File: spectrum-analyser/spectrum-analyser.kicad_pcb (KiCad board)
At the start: 2 copper layers, 37 parts, among them J1 Conn_Coaxial, J2 Conn_01x02, Q1 PMOS, Q2 PMOS, Q3 Q_NMOS_GSD, Q4 Q_NMOS_GSD, Q5 Q_PMOS_GSD, SW2 SW_UP, SW3 SW_RIGHT, SW4 SW_LEFT, SW5 SW_DOWN, SW6 SW_SPDT, U1 1.3" OLED, U2 LM1117MP-3.3, U3 ESP32-C3_Zero, U4 RX5808(V3.3), U5 AP9101CK6, U6 MCP73831-2-OT

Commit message: Improve PCB layout
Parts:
- JP1: value SolderJumper_2_Open -> BAT_PROT_BYPASS; footprint Jumper:SolderJumper-2_P1.3mm_Open_RoundedPad1.0x1.5mm -> Jumper:SolderJumper-3_P1.3mm_Open_RoundedPad1.0x1.5mm
- moved R8 144.8 mm to (102.5, 125.5)
- moved U6 144.8 mm to (99.5, 125.5)
- moved J2 134.9 mm to (99.0, 100.2), turned to 0 degrees
- moved JP1 131.4 mm to (99.0, 106.5)
- moved F1 126.8 mm to (105.5, 107.5), turned to 180 degrees
- moved Q4 124.1 mm to (101.5, 113.0), turned to -90 degrees
- moved R7 121.8 mm to (105.5, 111.0), turned to 0 degrees
- moved R6 121.0 mm to (105.5, 119.0), turned to 0 degrees
- moved Q5 119.6 mm to (101.5, 117.0)
- moved C3 119.3 mm to (105.5, 113.0), turned to 0 degrees
- moved U5 118.6 mm to (105.5, 116.0), turned to 0 degrees
- moved TP1 114.8 mm to (129.0, 151.5)
- moved TP2 109.9 mm to (125.5, 121.0)
- moved TP3 109.7 mm to (125.5, 125.5)
- moved SW1 101.4 mm to (142.6, 79.0)
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- renumbered D3 to D1, D1 to D2, D2 to D3, Q5 to Q3, Q3 to Q4, Q4 to Q5, R7 to R1, R8 to R3, R1 to R4, R3 to R5, R4 to R6, R5 to R7, R6 to R8, SW6 to SW1, U3 to U2, U2 to U3
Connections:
- C3 pad 1: -BATT -> -BAT_PROT
- JP1 pad 1: -BATT -> -BAT_PROT
- JP1 pad 2: GND -> -BATT
- Q4 pad 2: -BATT -> -BAT_PROT
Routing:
- added copper zone on B.Cu, net GND
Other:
- board outline added: 50 x 90 mm
- board text added: "3V3 REG"
- board text added: "BAT_PROT"
- board text added: "CHRG"
- board text added: "PCBWay max board size 50x110mm"
- board text added: "VUSB"
- board text removed: "PCBWay max board size"

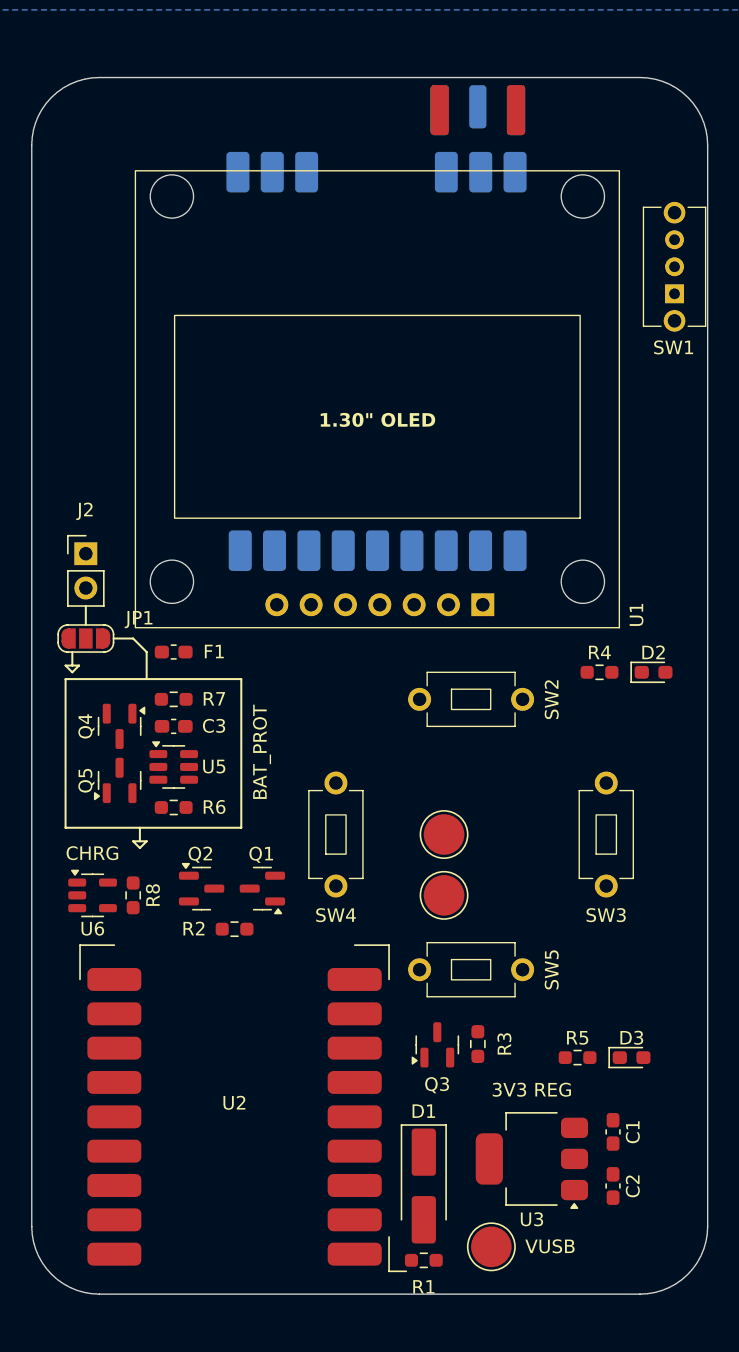
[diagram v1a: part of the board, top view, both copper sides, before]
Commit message: Add mounting holes
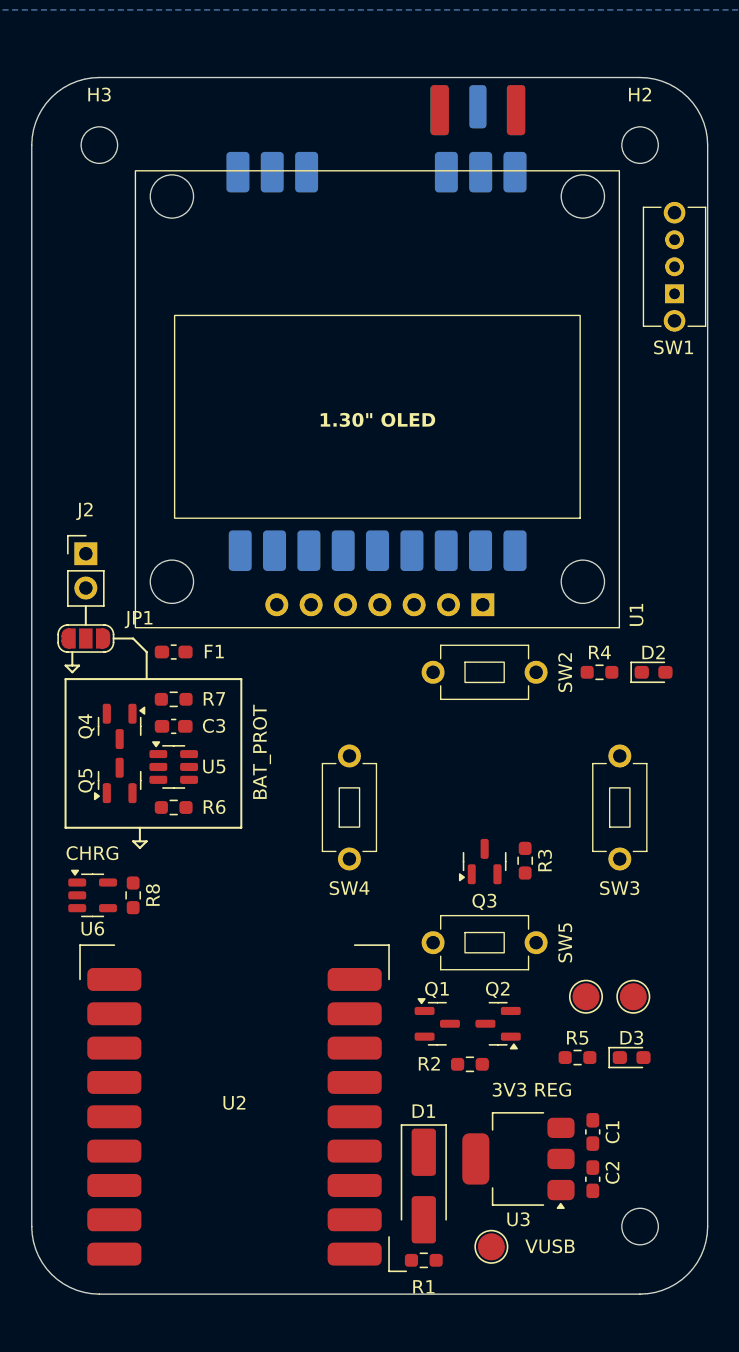
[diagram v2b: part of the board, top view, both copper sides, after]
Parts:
- added H1: MountingHole, MountingHole:MountingHole_2.7mm_M2.5, F.Cu at (140.0, 150.0)
- added H2: MountingHole, MountingHole:MountingHole_2.7mm_M2.5, F.Cu at (140.0, 70.0)
- added H3: MountingHole, MountingHole:MountingHole_2.7mm_M2.5, F.Cu at (100.0, 70.0)
- TP1, TP2, TP3: footprint TestPoint:TestPoint_Pad_D3.0mm -> TestPoint:TestPoint_Pad_D2.0mm
- moved Q1 20.1 mm to (125.0, 135.0)
- moved Q2 20.1 mm to (129.5, 135.0)
- moved R2 20.1 mm to (127.4, 138.0)
- moved TP2 15.9 mm to (136.0, 133.0)
- moved TP3 15.9 mm to (139.5, 133.0)
- moved Q3 14.0 mm to (128.5, 123.0)
- moved R3 14.0 mm to (131.5, 122.9)
- moved SW2 2.24 mm to (128.5, 109.0)
- moved SW3 2.24 mm to (138.5, 119.0)
- moved SW4 2.24 mm to (118.5, 119.0)
- moved SW5 2.24 mm to (128.5, 129.0)
- moved C2 1.58 mm to (136.5, 146.5)
- moved C1 1.50 mm to (136.5, 143.0)
- moved U3 1.00 mm to (131.0, 145.0)

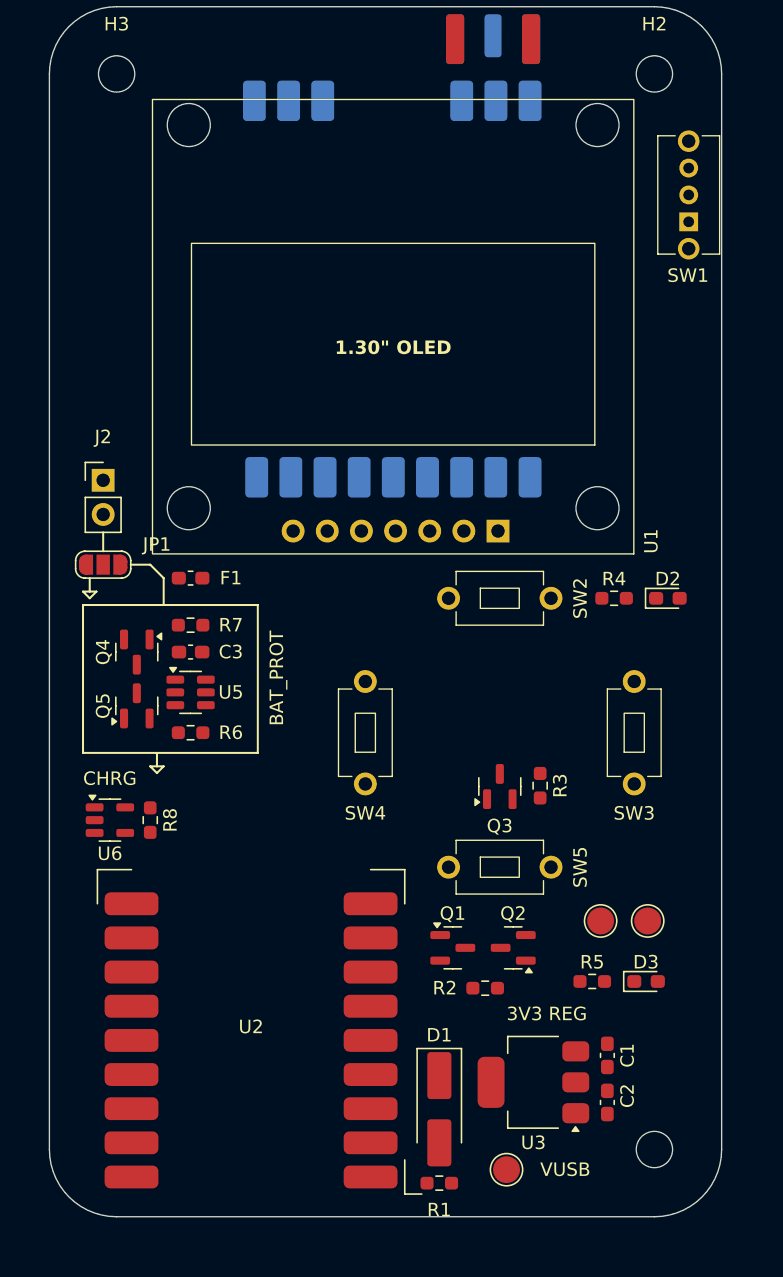
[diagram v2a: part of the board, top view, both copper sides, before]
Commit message: Improve component layout for spacing and round mechanical positions
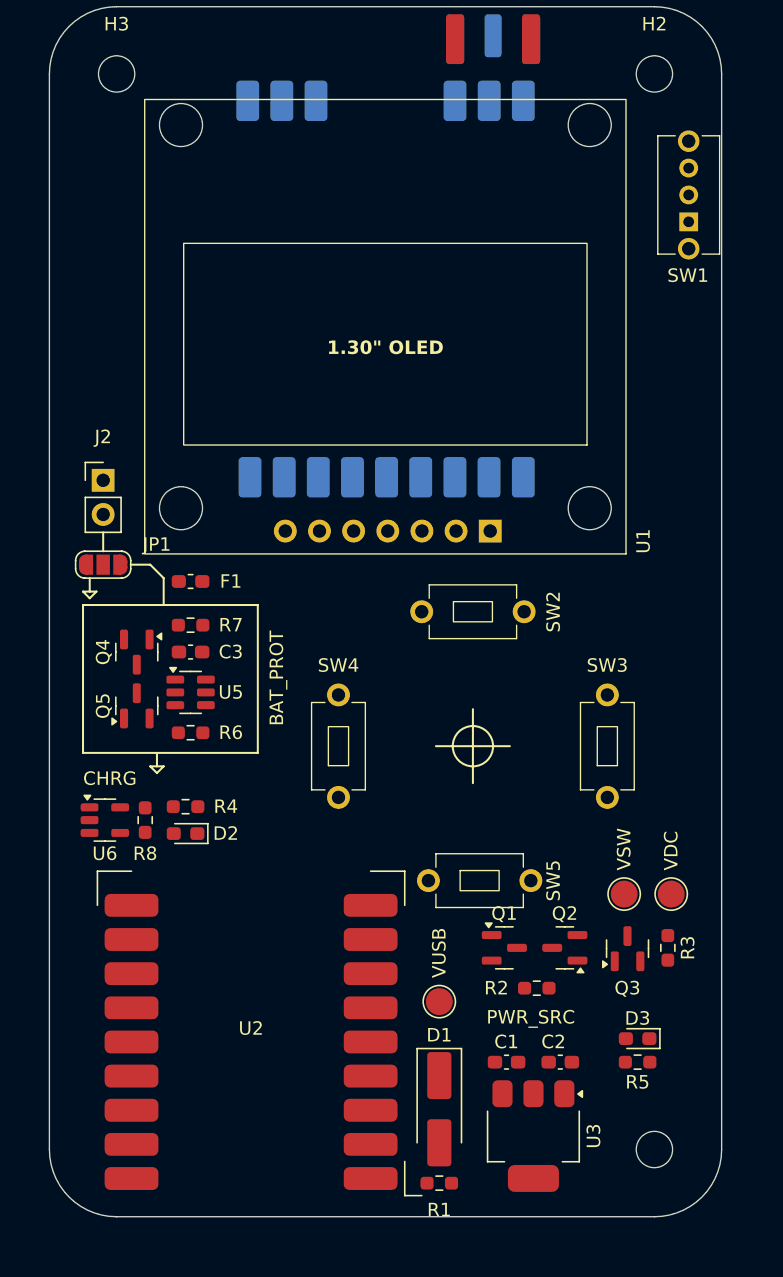
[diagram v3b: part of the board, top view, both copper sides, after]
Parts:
- moved D2 39.9 mm to (105.1, 126.5), turned to 180 degrees
- moved R4 35.4 mm to (105.1, 124.5)
- moved Q3 15.4 mm to (138.0, 135.1)
- moved R3 15.4 mm to (141.0, 135.0)
- moved TP1 13.5 mm to (124.0, 139.0)
- moved C1 7.52 mm to (129.0, 143.5), turned to 0 degrees
- moved R5 6.88 mm to (138.8, 143.5)
- moved TP2 5.62 mm to (141.2, 131.0)
- moved C2 4.61 mm to (133.0, 143.5), turned to 0 degrees
- moved D3 4.30 mm to (138.8, 141.8), turned to 180 degrees
- moved U3 4.00 mm to (131.0, 149.0), turned to -90 degrees
- moved Q1 3.84 mm to (128.8, 135.0)
- moved Q2 3.84 mm to (133.3, 135.0)
- moved R2 3.84 mm to (131.2, 138.0)
- moved TP3 2.66 mm to (137.8, 131.0)
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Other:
- board text added: "PWR_SRC"
- board text added: "VDC"
- board text added: "VSW"
- board text removed: "3V3 REG"

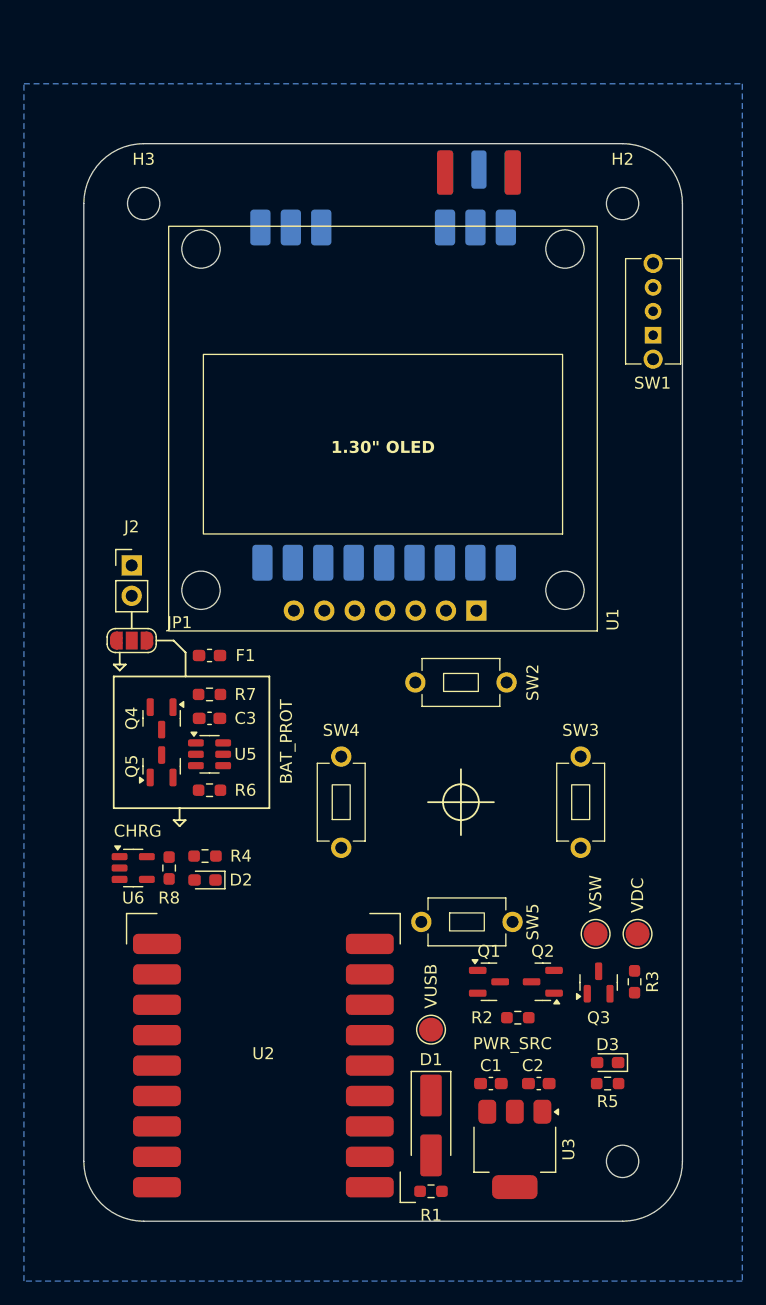
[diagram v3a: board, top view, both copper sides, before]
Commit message: Modify layout to group power and battery, increase board length by 5mm
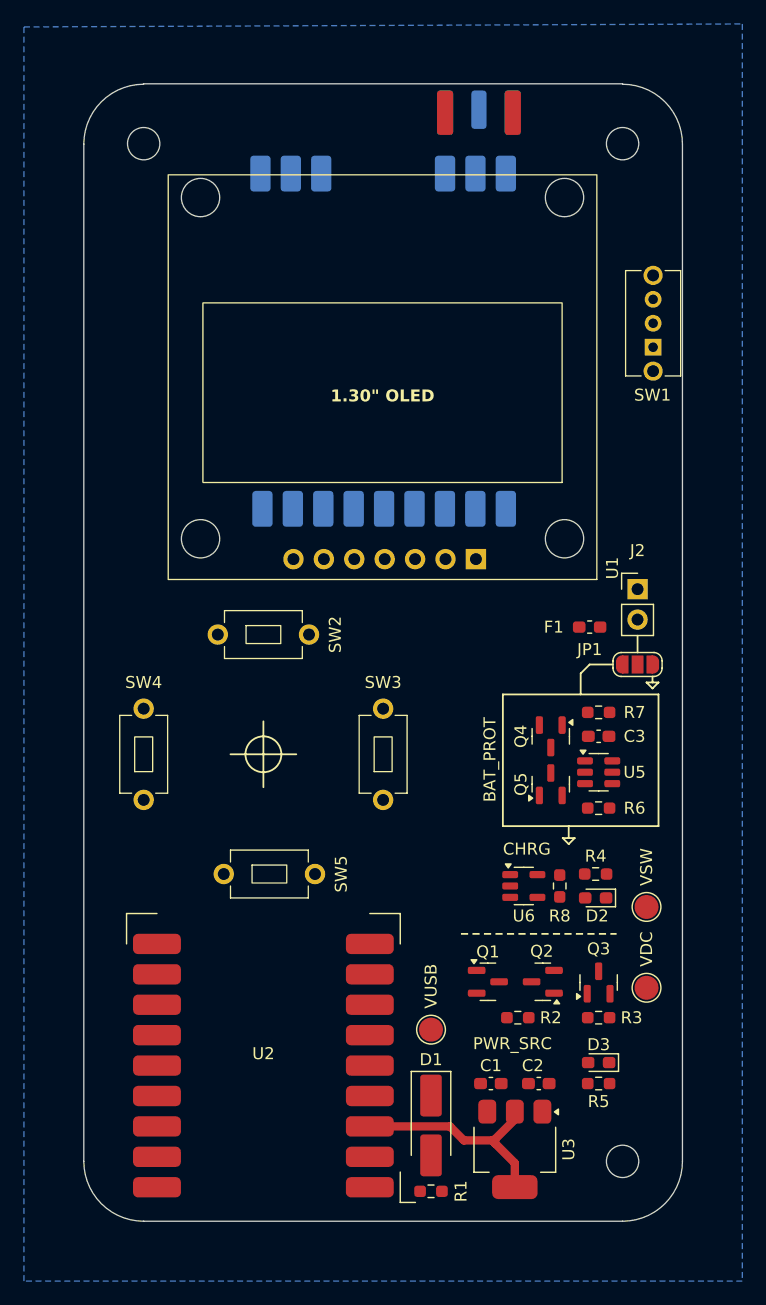
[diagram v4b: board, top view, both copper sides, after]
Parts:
- moved JP1 42.3 mm to (141.2, 108.5), turned to 0 degrees
- moved J2 42.3 mm to (141.2, 102.2)
- moved D2 32.7 mm to (137.8, 128.0)
- moved R4 32.7 mm to (137.8, 126.0)
- moved R8 32.7 mm to (134.8, 127.0)
- moved U6 32.7 mm to (131.8, 127.0)
- moved C3 32.5 mm to (138.0, 114.5)
- moved Q4 32.5 mm to (134.0, 114.5)
- moved Q5 32.5 mm to (134.0, 118.5)
- moved R6 32.5 mm to (138.0, 120.5)
- moved R7 32.5 mm to (138.0, 112.5)
- moved U5 32.5 mm to (138.0, 117.5)
- moved F1 31.8 mm to (137.2, 105.4), turned to 0 degrees
- moved SW2 17.0 mm to (110.0, 106.0)
- moved SW3 17.0 mm to (120.0, 116.0)
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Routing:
- net +3V3: track 0.00 -> 18.7 mm
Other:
- board size 50 x 90 mm -> 50 x 95 mm
